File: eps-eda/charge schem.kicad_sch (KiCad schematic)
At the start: 24 parts, among them J1 USB_C_Receptacle, J2 436500212, U5 MAX77757JEFG435+, U6 MAX17055EWL+T

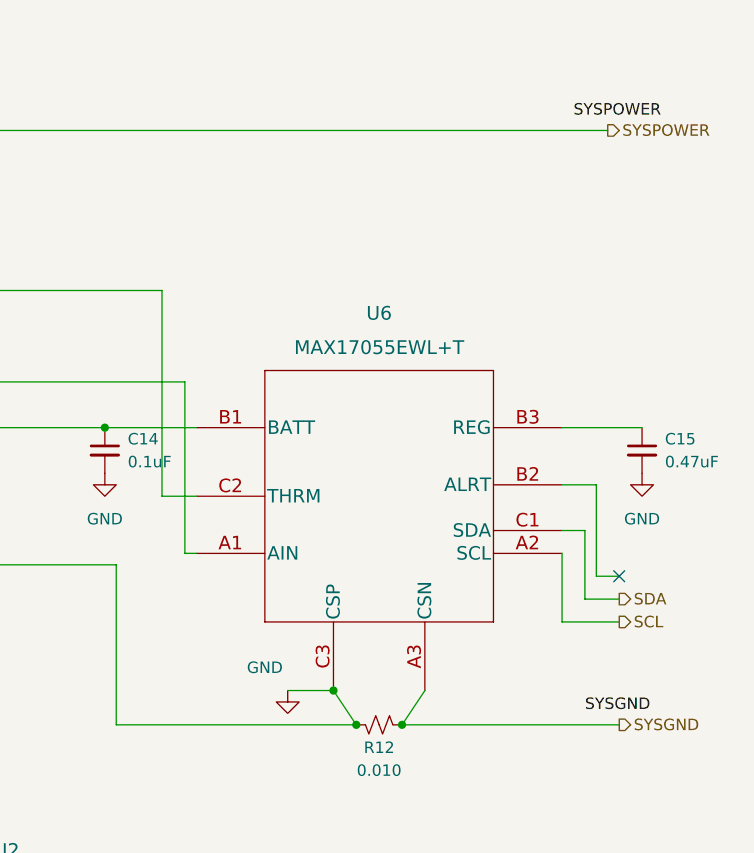
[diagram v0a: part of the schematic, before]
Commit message: rev 0.2 update
added 90deg pic adapter to include an edge cutout.

changed footprint of fuel gauge to implement ALRT signal.

rotated battery connector to better implement with the battery board.

Co-Authored-By: ajbrannigan <91212154+ajbrannigan@users.noreply.github.com>
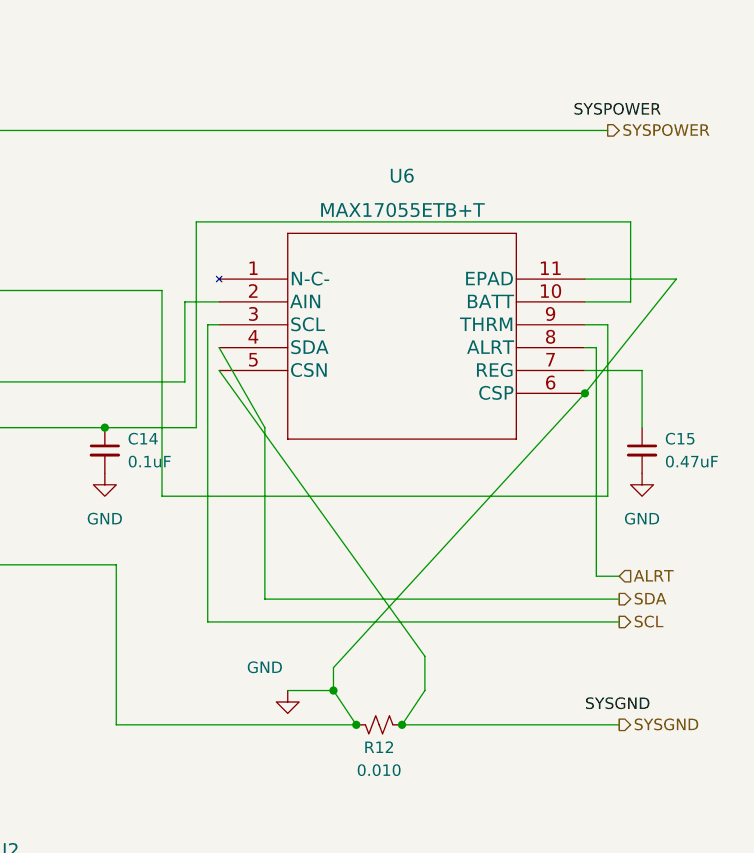
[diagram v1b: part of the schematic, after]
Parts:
- U6: value MAX17055EWL+T -> MAX17055ETB+T; footprint max17055:MAX17055EWL_plus_T -> max17055 smd:MAX17055ETB&plus_T; symbol MAX17055:MAX17055EWL+T -> max17055 smd:MAX17055ETB+T
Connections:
- net GND: now also U6.11 (EPAD), U6.6 (CSP); no longer U6.C3 (CSP)
- net SCL: now also U6.3 (SCL); no longer U6.A2 (SCL)
- net SDA: now also U6.4 (SDA); no longer U6.C1 (SDA)
- net SYSGND: now also U6.5 (CSN); no longer U6.A3 (CSN)
- net V_BAT: now also U6.10 (BATT); no longer U6.B1 (BATT)
- net at R11.2, TH1.1, U5.11 (THM): now also U6.2 (AIN); no longer U6.A1 (AIN)
- net at C15.1: now also U6.7 (REG); no longer U6.B3 (REG)
- net at C7.1, R11.1, U5.17 (PVL): now also U6.9 (THRM); no longer U6.C2 (THRM)
- new net ALRT: U6.8 (ALRT)
- no-connect marks 14 -> 13
